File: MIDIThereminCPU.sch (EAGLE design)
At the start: 15 parts, among them IC1 UA78M05DCY, J1 DCJ0202, Q1 16MHz, U1 ATMEGA328P-AU

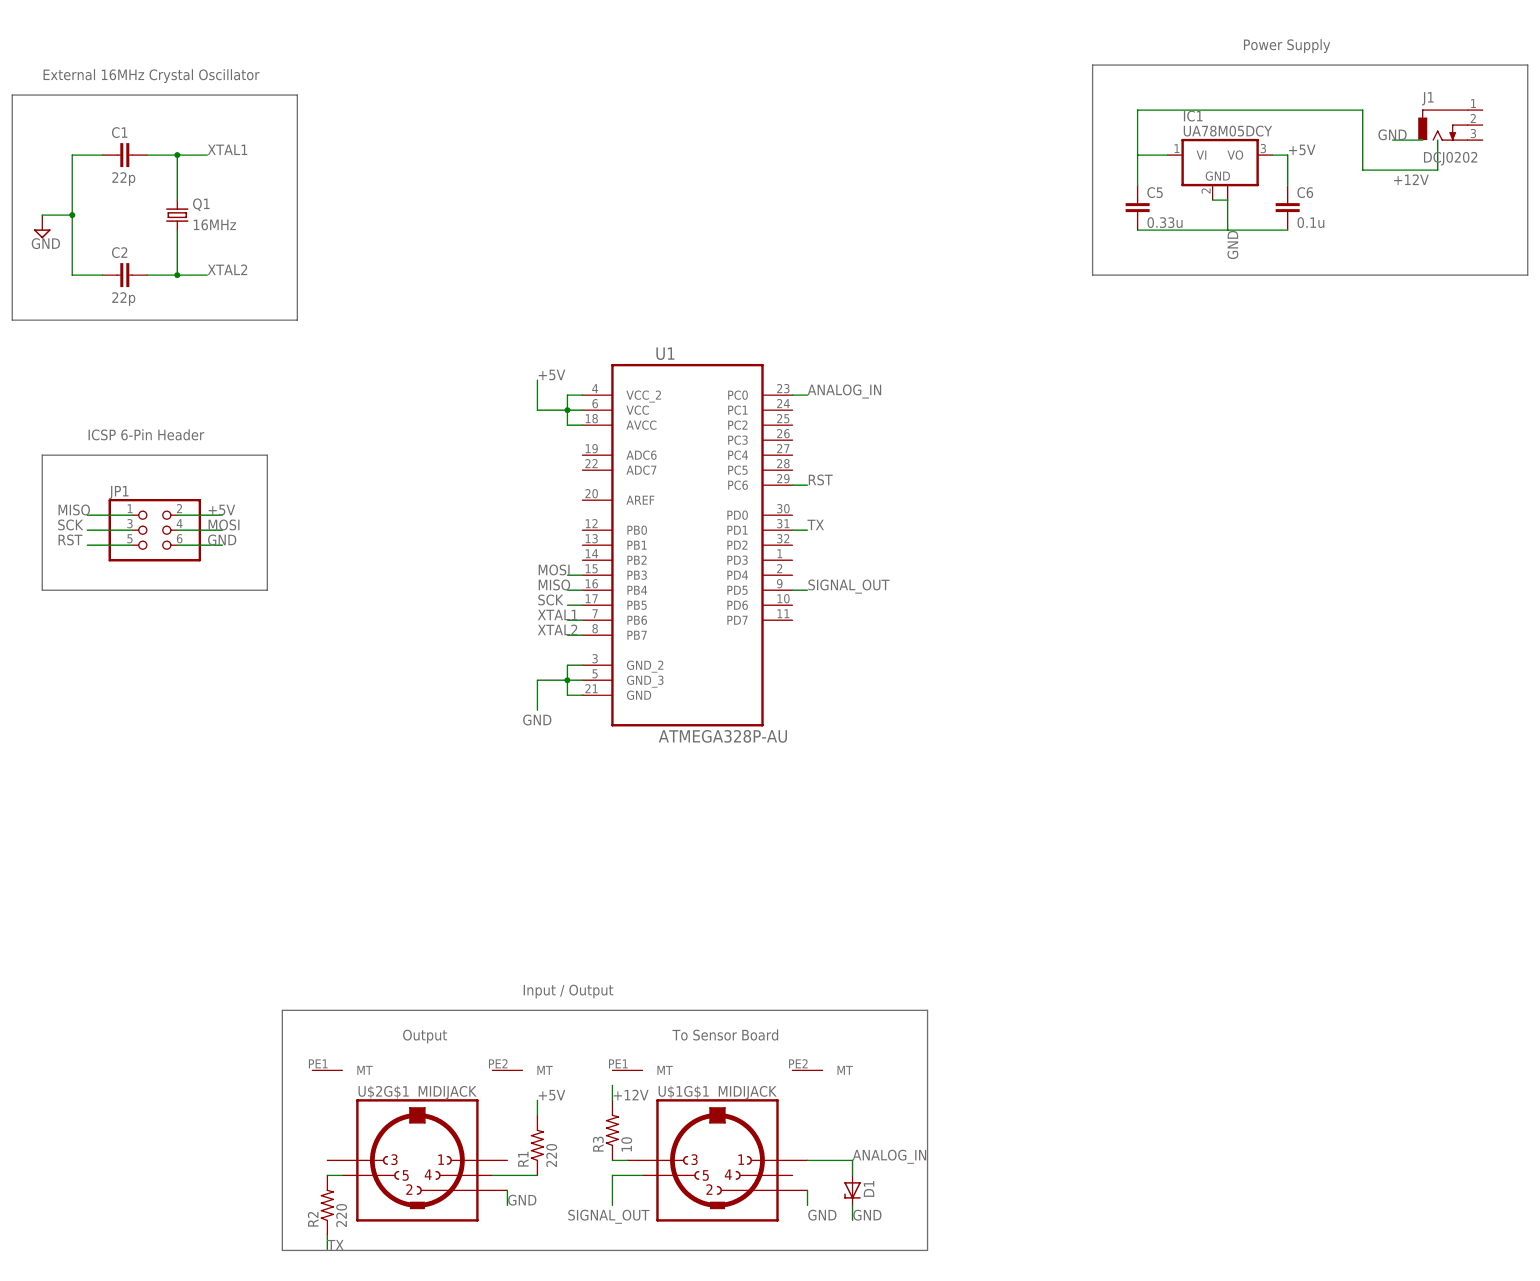
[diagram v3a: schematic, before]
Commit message: Added LED and push button, MIDI hookup refinement.
Added a 7-seg LED display and debounced push button. Grounded MIDI shields and added optional ferrite beads to MIDI out as per MIDI 2014 specifications.
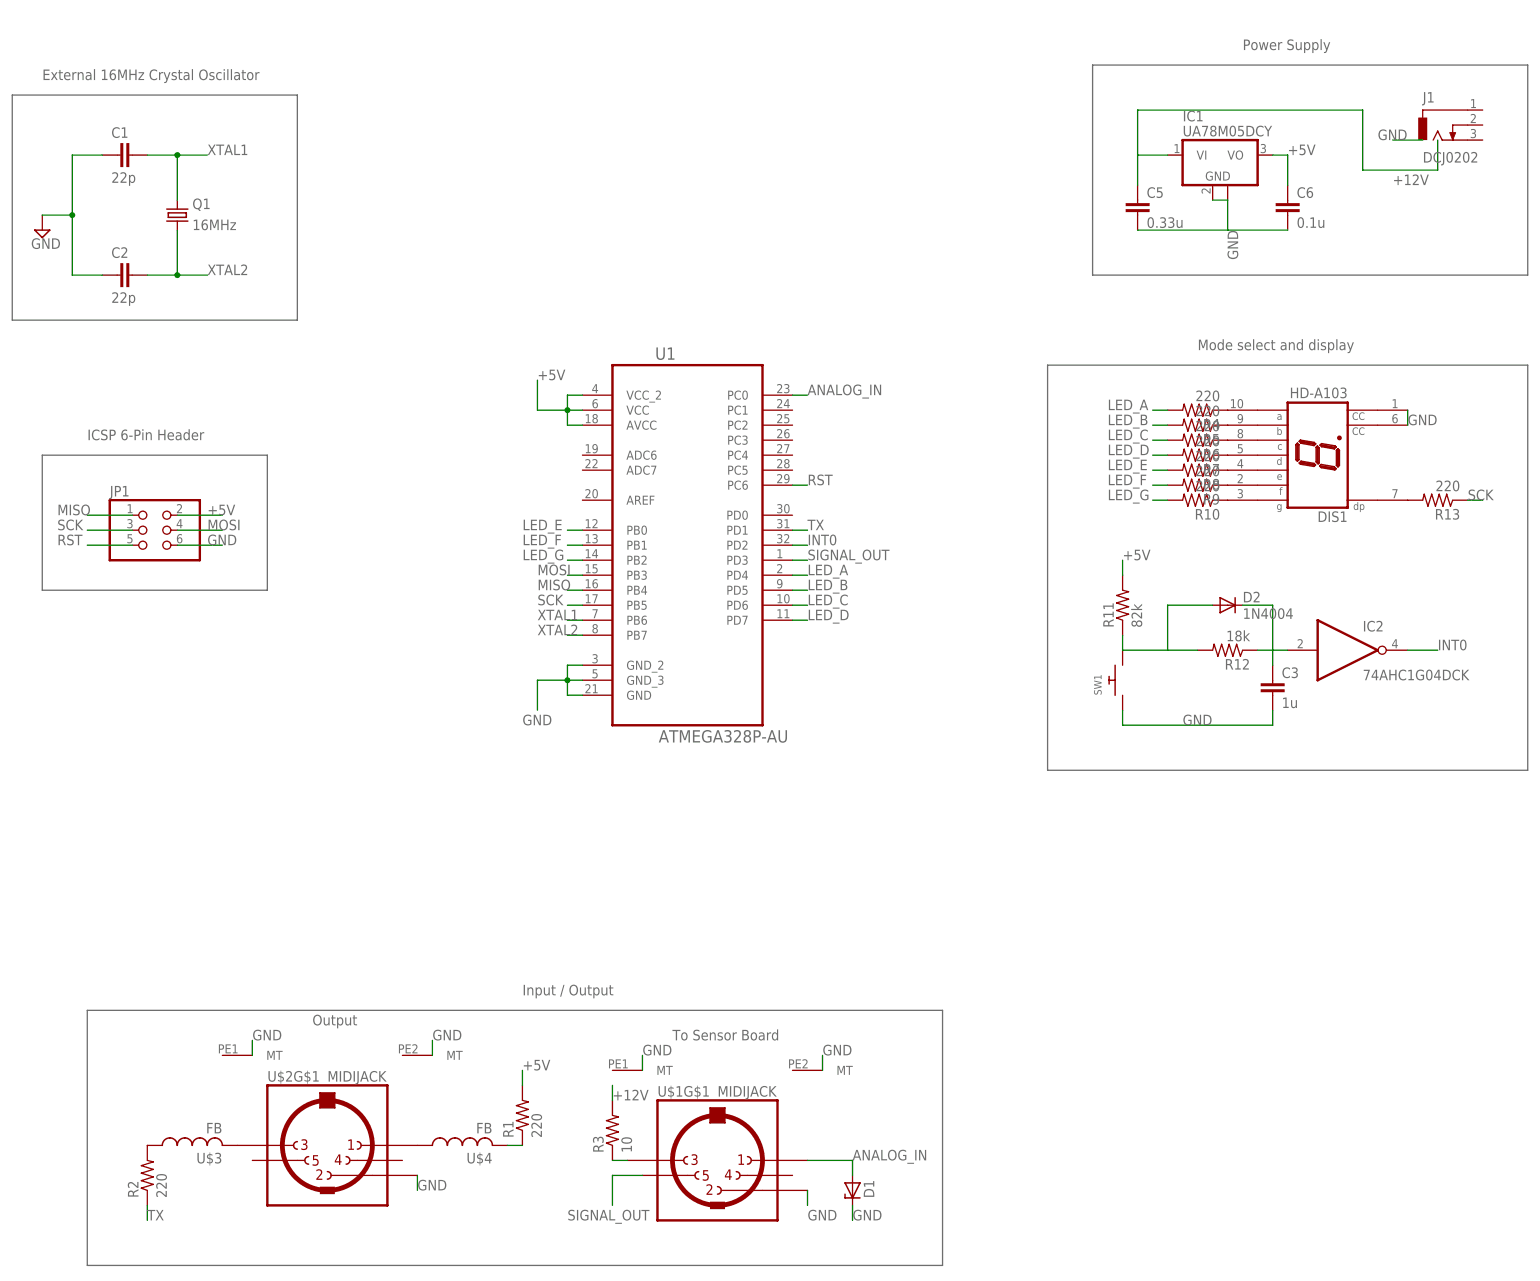
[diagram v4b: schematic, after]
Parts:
- added C3: 1u, capacitor-wima:C2,5-3
- added D2: 1N4004, diode:1N4004
- added DIS1: HD-A103, display-hp:HD-A103
- added IC2: 74AHC1G04DCK, 74xx-little-us:74AHC1G04DCK
- added R10, R13, R4, R5, R6, R7, R8, R9: 220, resistor:R-US_0207/10
- added R11: 82k, resistor:R-US_0207/10
- added R12: 18k, resistor:R-US_0207/10
- added SW1: (no value), adafruit:SWITCH_PUSHBUTTONSOFTTOUCHSMD_SJ
- added U$3, U$4: FB, adafruit:FB
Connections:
- new net INT0: IC2A.O, U1.PD2
- new net LED_A: R4.2, U1.PD4
- new net LED_B: R5.2, U1.PD5
- new net LED_C: R6.2, U1.PD6
- new net LED_D: R7.2, U1.PD7
- new net LED_E: R8.2, U1.PB0
- new net LED_F: R9.2, U1.PB1
- new net LED_G: R10.2, U1.PB2
- new net N$10: DIS1.G, R10.1
- new net N$11: D2.A, R11.1, R12.2, SW1.P$2
- new net N$12: U$2G$1.3, U$3.2
- new net N$13: R2.2, U$3.1
- new net N$14: C3.1, D2.C, IC2A.I, R12.1
- new net N$19: DIS1.DP, R13.2
- new net N$4: DIS1.A, R4.1
- new net N$5: DIS1.B, R5.1
- new net N$6: DIS1.C, R6.1
- new net N$7: DIS1.D, R7.1
- new net N$8: DIS1.E, R8.1
- new net N$9: DIS1.F, R9.1
- net +5V: now also R11.2
- net GND: now also C3.2, DIS1.CC, DIS1.CC@1, SW1.P$1
- net N$1: now also U$2G$1.1, U$4.1; no longer R1.1, U$2G$1.4
- net N$2: now also R1.1, U$4.2; no longer R2.2, U$2G$1.5
- net SCK: now also R13.1
- net SIGNAL_OUT: now also U1.PD3; no longer U1.PD5
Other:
- note added: "Mode select and display"
- moved on the sheet: R1, R2, U$2G$1

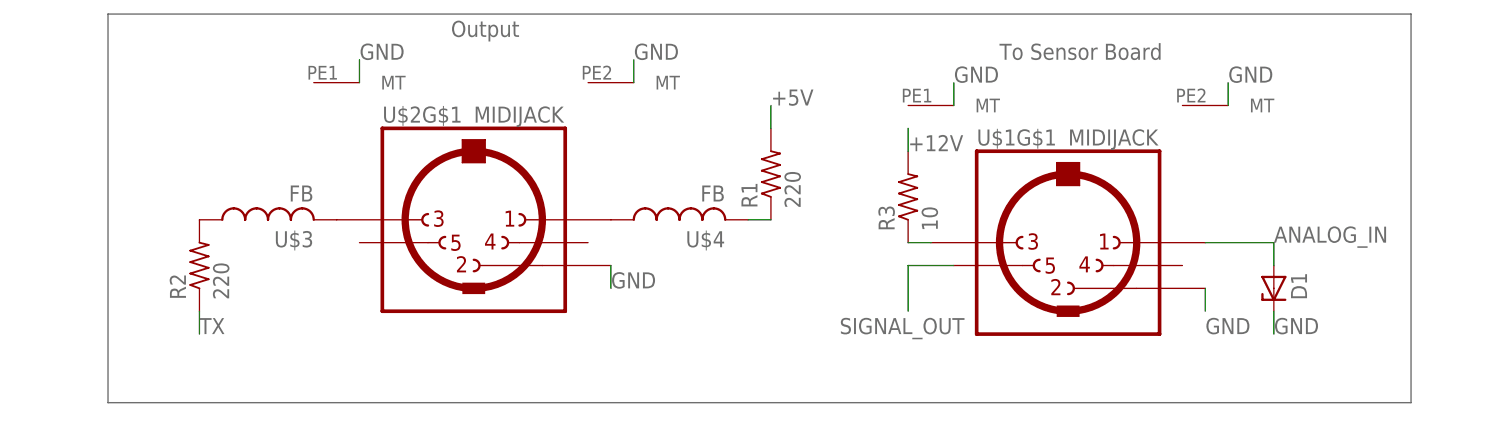
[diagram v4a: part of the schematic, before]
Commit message: Fixed some part connections
Changed midi output signals from pins 1 and 3 to 4 and 5. Reversed orientation of zener diode on MIDI in.
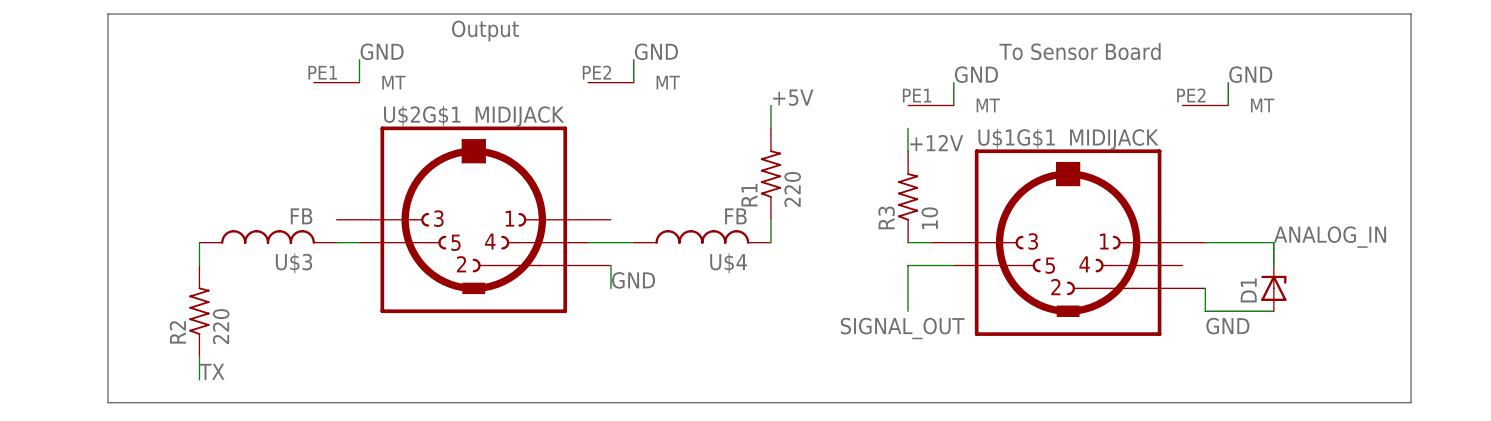
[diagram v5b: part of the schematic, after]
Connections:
- removed net N$12 (its old number): U$2G$1.3, U$3.2
- new net N$3: U$2G$1.5, U$3.2
- net ANALOG_IN: now also D1.C; no longer D1.A
- net GND: now also D1.A; no longer D1.C
- net N$1: now also U$2G$1.4; no longer U$2G$1.1
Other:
- moved on the sheet: D1, R2, U$3, U$4
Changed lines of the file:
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@@
 <grid distance="0.1" unitdist="inch" unit="inch" style="lines" multiple="1" display="no" altdistance="0.01" altunitdist="inch" altunit="inch"/>
 <layers>
-<layer number="1" name="Top" color="4" fill="1" visible="yes" active="no"/>
-<layer number="16" name="Bottom" color="1" fill="1" visible="yes" active="no"/>
-<layer number="17" name="Pads" color="2" fill="1" visible="yes" active="no"/>
-<layer number="18" name="Vias" color="2" fill="1" visible="yes" active="no"/>
-<layer number="19" name="Unrouted" color="6" fill="1" visible="yes" active="no"/>
-<layer number="20" name="Dimension" color="15" fill="1" visible="yes" active="no"/>
-<layer number="21" name="tPlace" color="7" fill="1" visible="yes" active="no"/>
-<layer number="22" name="bPlace" color="7" fill="1" visible="yes" active="no"/>
-<layer number="23" name="tOrigins" color="15" fill="1" visible="yes" active="no"/>
-<layer number="24" name="bOrigins" color="15" fill="1" visible="yes" active="no"/>
-<layer number="25" name="tNames" color="7" fill="1" visible="yes" active="no"/>
-<layer number="26" name="bNames" color="7" fill="1" visible="yes" active="no"/>
-<layer number="27" name="tValues" color="7" fill="1" visible="yes" active="no"/>
-<layer number="28" name="bValues" color="7" fill="1" visible="yes" active="no"/>
+<layer number="1" name="Top" color="4" fill="1" visible="no" active="no"/>
+<layer number="16" name="Bottom" color="1" fill="1" visible="no" active="no"/>
+<layer number="17" name="Pads" color="2" fill="1" visible="no" active="no"/>
+<layer number="18" name="Vias" color="2" fill="1" visible="no" active="no"/>
+<layer number="19" name="Unrouted" color="6" fill="1" visible="no" active="no"/>
+<layer number="20" name="Dimension" color="15" fill="1" visible="no" active="no"/>
+<layer number="21" name="tPlace" color="7" fill="1" visible="no" active="no"/>
+<layer number="22" name="bPlace" color="7" fill="1" visible="no" active="no"/>
+<layer number="23" name="tOrigins" color="15" fill="1" visible="no" active="no"/>
+<layer number="24" name="bOrigins" color="15" fill="1" visible="no" active="no"/>
+<layer number="25" name="tNames" color="7" fill="1" visible="no" active="no"/>
+<layer number="26" name="bNames" color="7" fill="1" visible="no" active="no"/>
+<layer number="27" name="tValues" color="7" fill="1" visible="no" active="no"/>
+<layer number="28" name="bValues" color="7" fill="1" visible="no" active="no"/>
 <layer number="29" name="tStop" color="7" fill="3" visible="no" active="no"/>
 <layer number="30" name="bStop" color="7" fill="6" visible="no" active="no"/>
@@
 <layer number="35" name="tGlue" color="7" fill="4" visible="no" active="no"/>
 <layer number="36" name="bGlue" color="7" fill="5" visible="no" active="no"/>
-<layer number="37" name="tTest" color="7" fill="1" visible="yes" active="no"/>
-<layer number="38" name="bTest" color="7" fill="1" visible="yes" active="no"/>
+<layer number="37" name="tTest" color="7" fill="1" visible="no" active="no"/>
+<layer number="38" name="bTest" color="7" fill="1" visible="no" active="no"/>
 <layer number="39" name="tKeepout" color="4" fill="11" visible="no" active="no"/>
 <layer number="40" name="bKeepout" color="1" fill="11" visible="no" active="no"/>
@@
 <layer number="44" name="Drills" color="7" fill="1" visible="no" active="no"/>
 <layer number="45" name="Holes" color="7" fill="1" visible="no" active="no"/>
-<layer number="46" name="Milling" color="3" fill="1" visible="yes" active="no"/>
-<layer number="47" name="Measures" color="7" fill="1" visible="yes" active="no"/>
-<layer number="48" name="Document" color="7" fill="1" visible="yes" active="no"/>
-<layer number="49" name="Reference" color="7" fill="1" visible="yes" active="no"/>
-<layer number="50" name="dxf" color="7" fill="1" visible="yes" active="no"/>
-<layer number="51" name="tDocu" color="7" fill="1" visible="yes" active="no"/>
-<layer number="52" name="bDocu" color="7" fill="1" visible="yes" active="no"/>
-<layer number="53" name="tGND_GNDA" color="7" fill="9" visible="yes" active="no"/>
-<layer number="54" name="bGND_GNDA" color="1" fill="9" visible="yes" active="no"/>
-<layer number="56" name="wert" color="7" fill="1" visible="yes" active="no"/>
-<layer number="57" name="tCAD" color="7" fill="1" visible="yes" active="no"/>
-<layer number="59" name="tCarbon" color="7" fill="1" visible="yes" active="no"/>
-<layer number="60" name="bCarbon" color="7" fill="1" visible="yes" active="no"/>
+<layer number="46" name="Milling" color="3" fill="1" visible="no" active="no"/>
+<layer number="47" name="Measures" color="7" fill="1" visible="no" active="no"/>
+<layer number="48" name="Document" color="7" fill="1" visible="no" active="no"/>
+<layer number="49" name="Reference" color="7" fill="1" visible="no" active="no"/>
+<layer number="50" name="dxf" color="7" fill="1" visible="no" active="no"/>
+<layer number="51" name="tDocu" color="7" fill="1" visible="no" active="no"/>
+<layer number="52" name="bDocu" color="7" fill="1" visible="no" active="no"/>
+<layer number="53" name="tGND_GNDA" color="7" fill="9" visible="no" active="no"/>
+<layer number="54" name="bGND_GNDA" color="1" fill="9" visible="no" active="no"/>
+<layer number="56" name="wert" color="7" fill="1" visible="no" active="no"/>
+<layer number="57" name="tCAD" color="7" fill="1" visible="no" active="no"/>
+<layer number="59" name="tCarbon" color="7" fill="1" visible="no" active="no"/>
+<layer number="60" name="bCarbon" color="7" fill="1" visible="no" active="no"/>
 <layer number="90" name="Modules" color="5" fill="1" visible="yes" active="yes"/>
 <layer number="91" name="Nets" color="2" fill="1" visible="yes" active="yes"/>
@@
 <instance part="U$2" gate="G$5" x="81.28" y="35.56"/>
 <instance part="R1" gate="G$1" x="101.6" y="25.4" rot="R90"/>
-<instance part="R2" gate="G$1" x="38.1" y="15.24" rot="R90"/>
-<instance part="D1" gate="G$1" x="157.48" y="12.7" rot="R270"/>
+<instance part="R2" gate="G$1" x="38.1" y="10.16" rot="R90"/>
+<instance part="D1" gate="G$1" x="157.48" y="12.7" rot="R90"/>
 <instance part="R3" gate="G$1" x="116.84" y="22.86" rot="R90"/>
 <instance part="DIS1" gate="A" x="236.22" y="137.16" rot="R90"/>
@@
 <instance part="IC2" gate="A" x="241.3" y="104.14"/>
 <instance part="D2" gate="1" x="220.98" y="111.76"/>
-<instance part="U$3" gate="G$1" x="45.72" y="20.32" rot="R90"/>
-<instance part="U$4" gate="G$1" x="91.44" y="20.32" rot="R90"/>
+<instance part="U$3" gate="G$1" x="45.72" y="17.78" rot="R90"/>
+<instance part="U$4" gate="G$1" x="93.98" y="17.78" rot="R90"/>
 <instance part="R13" gate="G$1" x="256.54" y="129.54" rot="R180"/>
 </instances>
@@
 </segment>
 <segment>
-<pinref part="D1" gate="G$1" pin="C"/>
-<wire x1="157.48" y1="10.16" x2="157.48" y2="7.62" width="0.1524" layer="91"/>
-<label x="157.48" y="7.62" size="1.778" layer="95"/>
-</segment>
-<segment>
 <wire x1="254" y1="190.5" x2="248.92" y2="190.5" width="0.1524" layer="91"/>
 <label x="246.38" y="190.5" size="1.778" layer="95"/>
@@
 <wire x1="149.86" y1="12.7" x2="149.86" y2="10.16" width="0.1524" layer="91"/>
 <label x="149.86" y="7.62" size="1.778" layer="95"/>
+<pinref part="D1" gate="G$1" pin="A"/>
+<wire x1="157.48" y1="10.16" x2="149.86" y2="10.16" width="0.1524" layer="91"/>
 </segment>
 <segment>
@@
 <segment>
 <pinref part="R2" gate="G$1" pin="1"/>
-<wire x1="38.1" y1="10.16" x2="38.1" y2="7.62" width="0.1524" layer="91"/>
-<label x="38.1" y="7.62" size="1.778" layer="95"/>
-</segment>
-</net>
-<net name="N$3" class="0">
-<segment>
-<pinref part="R3" gate="G$1" pin="1"/>
-<pinref part="U$1" gate="G$1" pin="3"/>
-<wire x1="116.84" y1="17.78" x2="119.38" y2="17.78" width="0.1524" layer="91"/>
+<wire x1="38.1" y1="5.08" x2="38.1" y2="2.54" width="0.1524" layer="91"/>
+<label x="38.1" y="2.54" size="1.778" layer="95"/>
 </segment>
 </net>
@@
 <pinref part="U$1" gate="G$1" pin="1"/>
 <wire x1="149.86" y1="17.78" x2="157.48" y2="17.78" width="0.1524" layer="91"/>
-<pinref part="D1" gate="G$1" pin="A"/>
-<wire x1="157.48" y1="17.78" x2="157.48" y2="15.24" width="0.1524" layer="91"/>
 <label x="157.48" y="17.78" size="1.778" layer="95"/>
+<pinref part="D1" gate="G$1" pin="C"/>
+<wire x1="157.48" y1="15.24" x2="157.48" y2="17.78" width="0.1524" layer="91"/>
 </segment>
 </net>
@@
 </segment>
 </net>
-<net name="N$1" class="0">
-<segment>
-<pinref part="U$2" gate="G$1" pin="1"/>
-<pinref part="U$4" gate="G$1" pin="1"/>
-</segment>
-</net>
 <net name="N$2" class="0">
 <segment>
 <pinref part="R1" gate="G$1" pin="1"/>
 <pinref part="U$4" gate="G$1" pin="2"/>
-<wire x1="101.6" y1="20.32" x2="99.06" y2="20.32" width="0.1524" layer="91"/>
-</segment>
-</net>
-<net name="N$12" class="0">
-<segment>
-<pinref part="U$2" gate="G$1" pin="3"/>
-<pinref part="U$3" gate="G$1" pin="2"/>
+<wire x1="101.6" y1="20.32" x2="101.6" y2="17.78" width="0.1524" layer="91"/>
 </segment>
 </net>
@@
 <pinref part="U$3" gate="G$1" pin="1"/>
 <pinref part="R2" gate="G$1" pin="2"/>
+<wire x1="38.1" y1="17.78" x2="38.1" y2="15.24" width="0.1524" layer="91"/>
 </segment>
 </net>
@@
 </segment>
 </net>
+<net name="N$3" class="0">
+<segment>
+<pinref part="U$3" gate="G$1" pin="2"/>
+<pinref part="U$2" gate="G$1" pin="5"/>
+<wire x1="53.34" y1="17.78" x2="55.88" y2="17.78" width="0.1524" layer="91"/>
+</segment>
+</net>
+<net name="N$1" class="0">
+<segment>
+<pinref part="U$2" gate="G$1" pin="4"/>
+<pinref part="U$4" gate="G$1" pin="1"/>
+<wire x1="81.28" y1="17.78" x2="86.36" y2="17.78" width="0.1524" layer="91"/>
+</segment>
+</net>
+<net name="N$12" class="0">
+<segment>
+<pinref part="R3" gate="G$1" pin="1"/>
+<pinref part="U$1" gate="G$1" pin="3"/>
+<wire x1="116.84" y1="17.78" x2="119.38" y2="17.78" width="0.1524" layer="91"/>
+</segment>
+</net>
